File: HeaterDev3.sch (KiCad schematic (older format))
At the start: 27 parts, among them J1 USB_C_Receptacle_USB2.0, J9 Conn_01x04_Female, Q1 Q_NMOS_GSD, SW1 SW_SPST, U1 ATSAMD21E18A-MU, U2 FUSB302BMPX, U3 STS-30-DIS, U5 AP2112K-3.3

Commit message: Fixes and changes
Swapped USB
Changed heater to PA19
Removed APA102 and replaced with SK6812MINI on pin PA06
Changed soldermask clearence
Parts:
- removed D1: APA102, LED_SMD:LED_RGB_PLCC-6, symbol LED:APA102
- added D1: SK6812MINI, LED_SMD:LED_SK6812MINI_PLCC4_3.5x3.5mm_P1.75mm, symbol LED:SK6812MINI
- added R5, R6: 5.1k, Resistor_SMD:R_0603_1608Metric, symbol Device:R_Small
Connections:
- net labels added: NEOPIX_DAT
- wire segments 95 -> 102
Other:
- note added: "CC Resistors in case you just want to omit the PD chip."
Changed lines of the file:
@@
 Wire Wire Line
 	5050 3000 5000 3000
-$Comp
-L LED:APA102 D1
-U 1 1 5EA7B5CC
-P 2000 3600
-F 0 "D1" H 2150 3850 50  0000 C CNN
-F 1 "APA102" H 2150 3350 50  0000 C CNN
-F 2 "LED_SMD:LED_RGB_PLCC-6" H 2050 3300 50  0001 L TNN
-F 3 "http://www.led-color.com/upload/201506/APA102%20LED.pdf" H 2100 3225 50  0001 L TNN
-	1    2000 3600
-	1    0    0    -1
-$EndComp
 Wire Wire Line
 	3000 3300 2800 3300
 Wire Wire Line
 	2800 3300 2800 2850
-Wire Wire Line
-	3000 3500 2300 3500
-Wire Wire Line
-	3000 3600 2300 3600
-$Comp
-L power:+3V3 #PWR0105
-U 1 1 5EA810E9
-P 2000 3200
-F 0 "#PWR0105" H 2000 3050 50  0001 C CNN
-F 1 "+3V3" H 2050 3300 50  0000 L CNN
-F 2 "" H 2000 3200 50  0001 C CNN
-F 3 "" H 2000 3200 50  0001 C CNN
-	1    2000 3200
-	1    0    0    -1
-$EndComp
-Wire Wire Line
-	2000 3200 2000 3300
-$Comp
-L power:GND #PWR0106
-U 1 1 5EA82082
-P 2000 3950
-F 0 "#PWR0106" H 2000 3700 50  0001 C CNN
-F 1 "GND" H 2005 3777 50  0000 C CNN
-F 2 "" H 2000 3950 50  0001 C CNN
-F 3 "" H 2000 3950 50  0001 C CNN
-	1    2000 3950
-	1    0    0    -1
-$EndComp
-Wire Wire Line
-	2000 3900 2000 3950
 $Comp
 L Device:LED D2
@@
 	3450 -1600 3550 -1600
 Connection ~ 3450 -1600
+Text GLabel 3550 -1600 2    50   Input ~ 0
+D+
 Text GLabel 3550 -1700 2    50   Input ~ 0
-D+
-Text GLabel 3550 -1600 2    50   Input ~ 0
 D-
 $Comp
@@
 Wire Wire Line
 	5800 1200 5800 1250
-Text GLabel 2900 3700 0    50   Input ~ 0
+Text GLabel 4500 4300 2    50   Input ~ 0
 HEATER
 $Comp
@@
 Text Label 8600 4850 0    50   ~ 0
 COIL
+Text GLabel 3800 -2000 0    50   Input ~ 0
+CC2
+Text GLabel 3800 -2100 0    50   Input ~ 0
+CC1
+$Comp
+L Device:R_Small R5
+U 1 1 5EEB0FDB
+P 4000 -2100
+F 0 "R5" V 3900 -2100 50  0000 C CNN
+F 1 "5.1k" V 4000 -2100 31  0000 C CNN
+F 2 "Resistor_SMD:R_0603_1608Metric" H 4000 -2100 50  0001 C CNN
+F 3 "~" H 4000 -2100 50  0001 C CNN
+	1    4000 -2100
+	0    1    1    0
+$EndComp
+$Comp
+L Device:R_Small R6
+U 1 1 5EEB1A64
+P 4000 -2000
+F 0 "R6" V 4100 -2000 50  0000 C CNN
+F 1 "5.1k" V 4000 -2000 31  0000 C CNN
+F 2 "Resistor_SMD:R_0603_1608Metric" H 4000 -2000 50  0001 C CNN
+F 3 "~" H 4000 -2000 50  0001 C CNN
+	1    4000 -2000
+	0    1    1    0
+$EndComp
+Text Notes 4150 -1900 0    50   ~ 0
+CC Resistors in case you just want to omit the PD chip.
+$Comp
+L power:GND #PWR0138
+U 1 1 5EEB3038
+P 4200 -2100
+F 0 "#PWR0138" H 4200 -2350 50  0001 C CNN
+F 1 "GND" H 4205 -2273 50  0000 C CNN
+F 2 "" H 4200 -2100 50  0001 C CNN
+F 3 "" H 4200 -2100 50  0001 C CNN
+	1    4200 -2100
+	0    -1   -1   0
+$EndComp
+Wire Wire Line
+	4200 -2100 4150 -2100
+Wire Wire Line
+	4100 -2000 4150 -2000
+Wire Wire Line
+	4150 -2000 4150 -2100
+Connection ~ 4150 -2100
+Wire Wire Line
+	4150 -2100 4100 -2100
+Wire Wire Line
+	3900 -2100 3800 -2100
+Wire Wire Line
+	3900 -2000 3800 -2000
+$Comp
+L LED:SK6812MINI D1
+U 1 1 5EEF51C5
+P 1450 5400
+F 0 "D1" H 1794 5446 50  0000 L CNN
+F 1 "SK6812MINI" H 1794 5355 50  0000 L CNN
+F 2 "LED_SMD:LED_SK6812MINI_PLCC4_3.5x3.5mm_P1.75mm" H 1500 5100 50  0001 L TNN
+F 3 "https://cdn-shop.adafruit.com/product-files/2686/SK6812MINI_REV.01-1-2.pdf" H 1550 5025 50  0001 L TNN
+	1    1450 5400
+	1    0    0    -1
+$EndComp
+Text GLabel 2900 4100 0    50   Input ~ 0
+NEOPIX_DAT
+Wire Wire Line
+	3000 4100 2900 4100
+Wire Wire Line
+	4500 4300 4400 4300
+Text GLabel 1050 5400 0    50   Input ~ 0
+NEOPIX_DAT
+Wire Wire Line
+	1150 5400 1050 5400
+$Comp
+L power:GND #PWR0105
+U 1 1 5EF01523
+P 1450 5750
+F 0 "#PWR0105" H 1450 5500 50  0001 C CNN
+F 1 "GND" V 1455 5622 50  0000 R CNN
+F 2 "" H 1450 5750 50  0001 C CNN
+F 3 "" H 1450 5750 50  0001 C CNN
+	1    1450 5750
+	1    0    0    -1
+$EndComp
+$Comp
+L power:+3V3 #PWR0106
+U 1 1 5EF01E84
+P 1450 4900
+F 0 "#PWR0106" H 1450 4750 50  0001 C CNN
+F 1 "+3V3" V 1350 4650 50  0000 L CNN
+F 2 "" H 1450 4900 50  0001 C CNN
+F 3 "" H 1450 4900 50  0001 C CNN
+	1    1450 4900
+	1    0    0    -1
+$EndComp
+Wire Wire Line
+	1450 4900 1450 5100
+Wire Wire Line
+	1450 5700 1450 5750
 $EndSCHEMATC

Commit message: Added Temperature Cutoff Circuit
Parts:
- removed Q1: Q_NMOS_GSD, Package_TO_SOT_SMD:SOT-223-3_TabPin2, symbol Device:Q_NMOS_GSD
- added D3: LED, Capacitor_SMD:C_0603_1608Metric, symbol Device:LED
- added Q1: Q_NMOS_GDS, Package_TO_SOT_SMD:SOT-223-3_TabPin2, symbol Device:Q_NMOS_GDS
- added R10, R11, R12: 10k, Resistor_SMD:R_0603_1608Metric, symbol Device:R_Small
- added R13: 1.5k, Resistor_SMD:R_0603_1608Metric, symbol Device:R_Small
- added R7, R9: 4.7k, Resistor_SMD:R_0603_1608Metric, symbol Device:R_Small
- added R8: NTC, Resistor_SMD:R_0603_1608Metric, symbol Device:R_Small
- added U4: LM393, Package_DFN_QFN:DFN-8-1EP_2x2mm_P0.45mm_EP0.64x1.38mm, symbol Comparator:LM393
- R3, R4: value 1.5k -> 10k
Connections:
- net labels added: ELEMENT_GATE
- wire segments 102 -> 130
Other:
- note added: "3.024k at 60c\n10k at 25c\n2.2v vdiv when at 60c and R7 is 1.5k\nfor cutoff at 40 use 2.5k\nfor cutoff at 50 use 2k"
- note added: "TH voltage 2.2v"

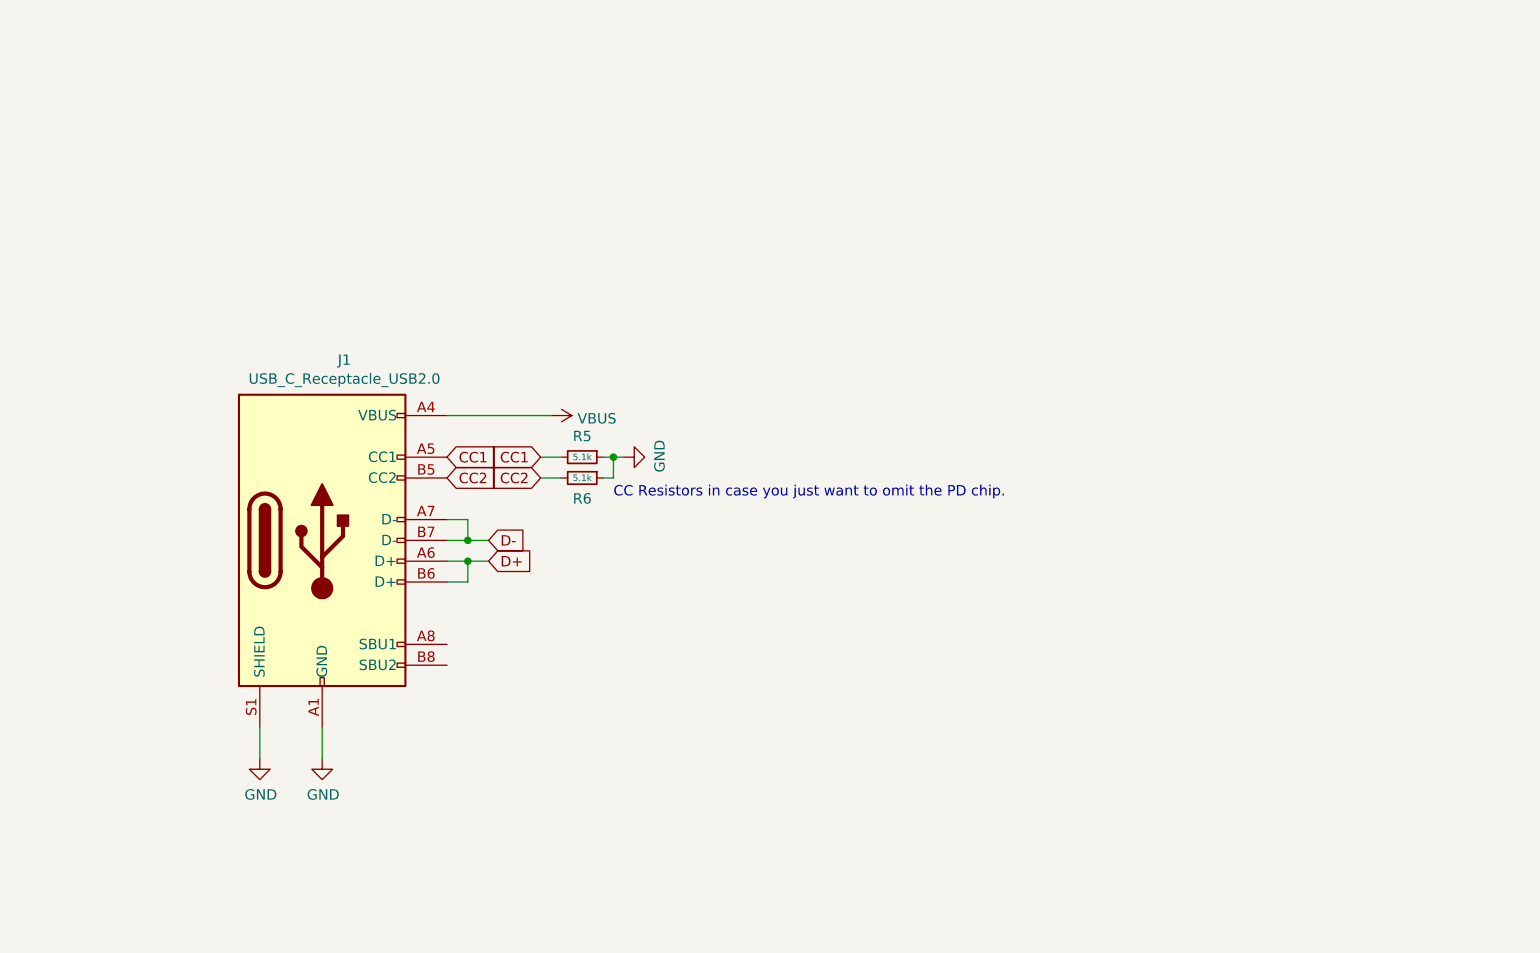
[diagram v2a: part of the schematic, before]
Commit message: Swapped out USB Connector for a simpler version.
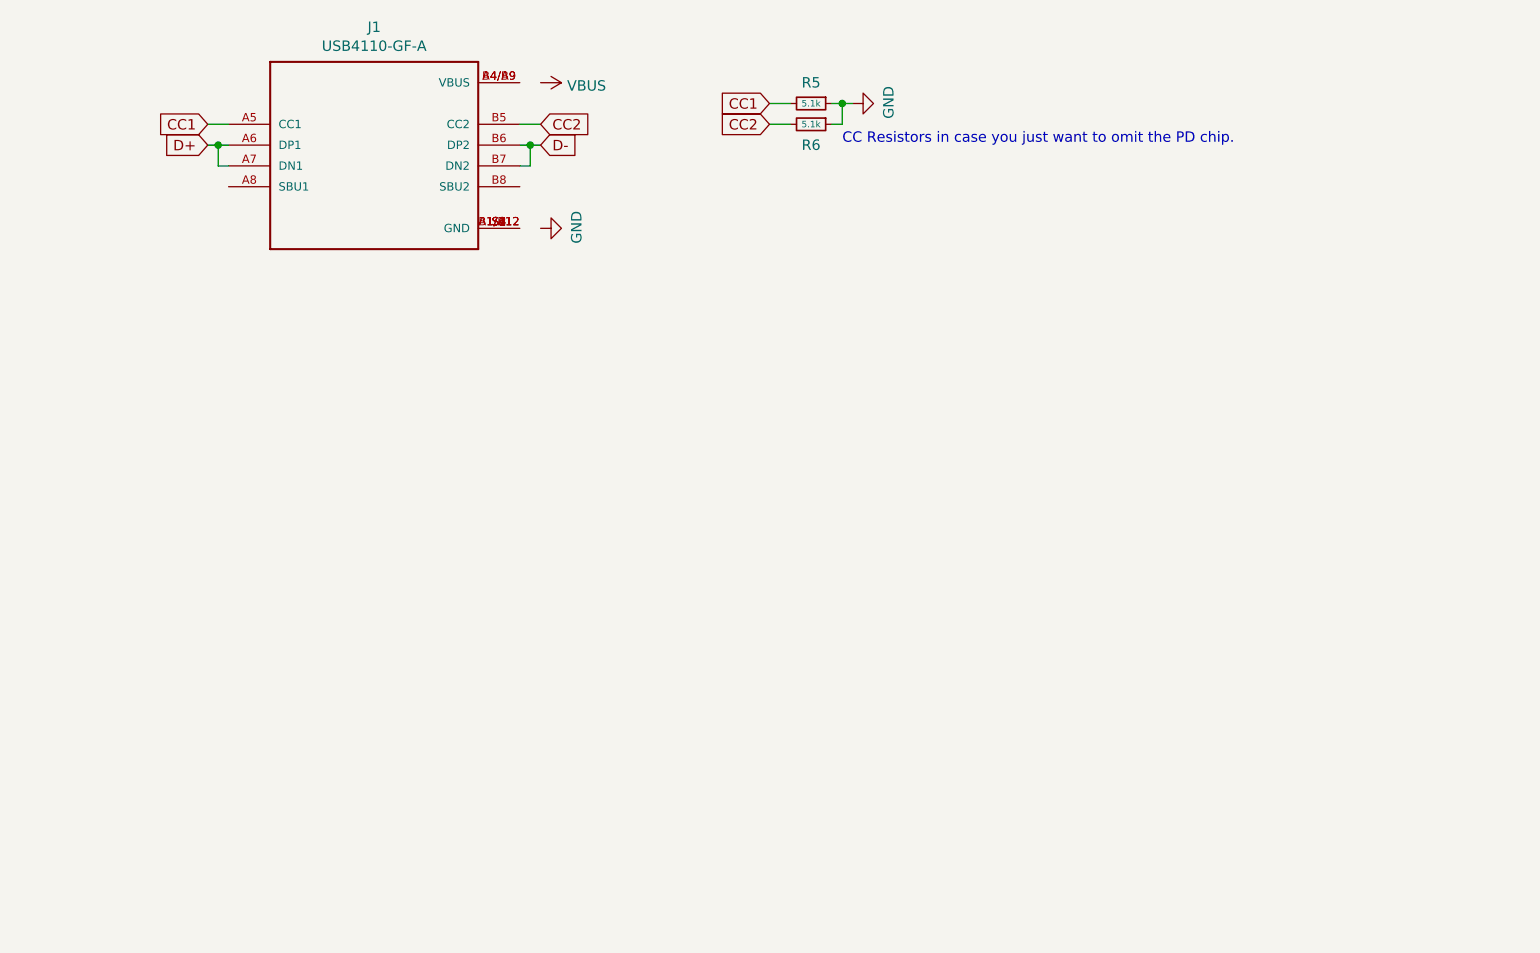
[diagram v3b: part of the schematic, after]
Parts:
- removed J1: USB_C_Receptacle_USB2.0, Connector_USB:USB_C_Receptacle_Amphenol_12401610E4-2A, symbol Connector:USB_C_Receptacle_USB2.0
- added J1: USB4110-GF-A, HeaterDev3:GCT_USB4110-GF-A, symbol USB4110-GF-A:USB4110-GF-A
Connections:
- wire segments 130 -> 129
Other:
- moved on the sheet: R5, R6
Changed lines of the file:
@@
 Connection ~ 10350 -1350
-$Comp
-L Connector:USB_C_Receptacle_USB2.0 J1
-U 1 1 5EAB43F1
-P 2750 -1700
-F 0 "J1" H 2857 -833 50  0000 C CNN
-F 1 "USB_C_Receptacle_USB2.0" H 2857 -924 50  0000 C CNN
-F 2 "Connector_USB:USB_C_Receptacle_Amphenol_12401610E4-2A" H 2900 -1700 50  0001 C CNN
-F 3 "https://www.usb.org/sites/default/files/documents/usb_type-c.zip" H 2900 -1700 50  0001 C CNN
-	1    2750 -1700
-	1    0    0    -1
-$EndComp
 $Comp
 L Device:C_Small C4
@@
 Text GLabel 2950 4300 0    50   Input ~ 0
 SDA
-Wire Wire Line
-	3350 -1800 3450 -1800
-Wire Wire Line
-	3450 -1800 3450 -1700
-Wire Wire Line
-	3450 -1700 3350 -1700
-Wire Wire Line
-	3450 -1600 3450 -1500
-Wire Wire Line
-	3350 -1500 3450 -1500
-Wire Wire Line
-	3350 -1600 3450 -1600
-Wire Wire Line
-	3450 -1700 3550 -1700
-Connection ~ 3450 -1700
-Wire Wire Line
-	3450 -1600 3550 -1600
-Connection ~ 3450 -1600
-Text GLabel 3550 -1600 2    50   Input ~ 0
-D+
-Text GLabel 3550 -1700 2    50   Input ~ 0
-D-
 $Comp
 L power:+3V3 #PWR0111
@@
 Wire Wire Line
 	10650 -1950 10650 -1850
-Text GLabel 3350 -2100 2    50   Input ~ 0
+Text GLabel 2200 -3700 0    50   Input ~ 0
 CC1
-Text GLabel 3350 -2000 2    50   Input ~ 0
+Text GLabel 3800 -3700 2    50   Input ~ 0
 CC2
 Text GLabel 2350 1250 2    50   Input ~ 0
@@
 Wire Wire Line
 	2900 3700 3000 3700
-$Comp
-L power:GND #PWR0124
-U 1 1 5EECBAEE
-P 2750 -650
-F 0 "#PWR0124" H 2750 -900 50  0001 C CNN
-F 1 "GND" H 2755 -823 50  0000 C CNN
-F 2 "" H 2750 -650 50  0001 C CNN
-F 3 "" H 2750 -650 50  0001 C CNN
-	1    2750 -650
-	1    0    0    -1
-$EndComp
-$Comp
-L power:GND #PWR0125
-U 1 1 5EECC53B
-P 2450 -650
-F 0 "#PWR0125" H 2450 -900 50  0001 C CNN
-F 1 "GND" H 2455 -823 50  0000 C CNN
-F 2 "" H 2450 -650 50  0001 C CNN
-F 3 "" H 2450 -650 50  0001 C CNN
-	1    2450 -650
-	1    0    0    -1
-$EndComp
-Wire Wire Line
-	2750 -800 2750 -650
-Wire Wire Line
-	2450 -800 2450 -650
 $Comp
 L Mechanical:MountingHole H3
@@
 L power:VBUS #PWR0112
 U 1 1 5ECB229D
-P 3850 -2300
-F 0 "#PWR0112" H 3850 -2450 50  0001 C CNN
-F 1 "VBUS" V 3865 -2173 50  0000 L CNN
-F 2 "" H 3850 -2300 50  0001 C CNN
-F 3 "" H 3850 -2300 50  0001 C CNN
-	1    3850 -2300
-	0    1    1    0
-$EndComp
-Wire Wire Line
-	3350 -2300 3850 -2300
+P 3800 -3900
+F 0 "#PWR0112" H 3800 -4050 50  0001 C CNN
+F 1 "VBUS" V 3815 -3773 50  0000 L CNN
+F 2 "" H 3800 -3900 50  0001 C CNN
+F 3 "" H 3800 -3900 50  0001 C CNN
+	1    3800 -3900
+	0    1    1    0
+$EndComp
 $Comp
 L Interface_USB:FUSB302BMPX U2
@@
 Text Label 8600 4850 0    50   ~ 0
 COIL
-Text GLabel 3800 -2000 0    50   Input ~ 0
+Text GLabel 4900 -3700 0    50   Input ~ 0
 CC2
-Text GLabel 3800 -2100 0    50   Input ~ 0
+Text GLabel 4900 -3800 0    50   Input ~ 0
 CC1
 $Comp
 L Device:R_Small R5
 U 1 1 5EEB0FDB
-P 4000 -2100
-F 0 "R5" V 3900 -2100 50  0000 C CNN
-F 1 "5.1k" V 4000 -2100 31  0000 C CNN
-F 2 "Resistor_SMD:R_0603_1608Metric" H 4000 -2100 50  0001 C CNN
-F 3 "~" H 4000 -2100 50  0001 C CNN
-	1    4000 -2100
+P 5100 -3800
+F 0 "R5" V 5000 -3800 50  0000 C CNN
+F 1 "5.1k" V 5100 -3800 31  0000 C CNN
+F 2 "Resistor_SMD:R_0603_1608Metric" H 5100 -3800 50  0001 C CNN
+F 3 "~" H 5100 -3800 50  0001 C CNN
+	1    5100 -3800
 	0    1    1    0
 $EndComp
@@
 L Device:R_Small R6
 U 1 1 5EEB1A64
-P 4000 -2000
-F 0 "R6" V 4100 -2000 50  0000 C CNN
-F 1 "5.1k" V 4000 -2000 31  0000 C CNN
-F 2 "Resistor_SMD:R_0603_1608Metric" H 4000 -2000 50  0001 C CNN
-F 3 "~" H 4000 -2000 50  0001 C CNN
-	1    4000 -2000
-	0    1    1    0
-$EndComp
-Text Notes 4150 -1900 0    50   ~ 0
+P 5100 -3700
+F 0 "R6" V 5200 -3700 50  0000 C CNN
+F 1 "5.1k" V 5100 -3700 31  0000 C CNN
+F 2 "Resistor_SMD:R_0603_1608Metric" H 5100 -3700 50  0001 C CNN
+F 3 "~" H 5100 -3700 50  0001 C CNN
+	1    5100 -3700
+	0    1    1    0
+$EndComp
+Text Notes 5250 -3600 0    50   ~ 0
 CC Resistors in case you just want to omit the PD chip.
 $Comp
 L power:GND #PWR0138
 U 1 1 5EEB3038
-P 4200 -2100
-F 0 "#PWR0138" H 4200 -2350 50  0001 C CNN
-F 1 "GND" H 4205 -2273 50  0000 C CNN
-F 2 "" H 4200 -2100 50  0001 C CNN
-F 3 "" H 4200 -2100 50  0001 C CNN
-	1    4200 -2100
+P 5300 -3800
+F 0 "#PWR0138" H 5300 -4050 50  0001 C CNN
+F 1 "GND" H 5305 -3973 50  0000 C CNN
+F 2 "" H 5300 -3800 50  0001 C CNN
+F 3 "" H 5300 -3800 50  0001 C CNN
+	1    5300 -3800
 	0    -1   -1   0
 $EndComp
 Wire Wire Line
-	4200 -2100 4150 -2100
-Wire Wire Line
-	4100 -2000 4150 -2000
-Wire Wire Line
-	4150 -2000 4150 -2100
-Connection ~ 4150 -2100
-Wire Wire Line
-	4150 -2100 4100 -2100
-Wire Wire Line
-	3900 -2100 3800 -2100
-Wire Wire Line
-	3900 -2000 3800 -2000
+	5300 -3800 5250 -3800
+Wire Wire Line
+	5200 -3700 5250 -3700
+Wire Wire Line
+	5250 -3700 5250 -3800
+Connection ~ 5250 -3800
+Wire Wire Line
+	5250 -3800 5200 -3800
+Wire Wire Line
+	5000 -3800 4900 -3800
+Wire Wire Line
+	5000 -3700 4900 -3700
 $Comp
 L LED:SK6812MINI D1
@@
 Wire Wire Line
 	7150 10200 7100 10200
+$Comp
+L USB4110-GF-A:USB4110-GF-A J1
+U 1 1 5EF03D48
+P 3000 -3600
+F 0 "J1" H 3000 -3033 50  0000 C CNN
+F 1 "USB4110-GF-A" H 3000 -3124 50  0000 C CNN
+F 2 "HeaterDev3:GCT_USB4110-GF-A" H 3000 -3600 50  0001 L BNN
+F 3 "" H 3000 -3600 50  0001 L BNN
+F 4 "A" H 3000 -3600 50  0001 L BNN "Field4"
+F 5 "GCT" H 3000 -3600 50  0001 L BNN "Field5"
+F 6 "Manufacturer Recommendations" H 3000 -3600 50  0001 L BNN "Field6"
+	1    3000 -3600
+	1    0    0    -1
+$EndComp
+Text GLabel 2200 -3600 0    50   Input ~ 0
+D+
+Text GLabel 3800 -3600 2    50   Input ~ 0
+D-
+Wire Wire Line
+	3700 -3700 3800 -3700
+Wire Wire Line
+	2200 -3700 2300 -3700
+Wire Wire Line
+	2300 -3600 2250 -3600
+Wire Wire Line
+	3800 -3600 3750 -3600
+Wire Wire Line
+	2250 -3600 2250 -3500
+Wire Wire Line
+	2250 -3500 2300 -3500
+Connection ~ 2250 -3600
+Wire Wire Line
+	2250 -3600 2200 -3600
+Wire Wire Line
+	3700 -3500 3750 -3500
+Wire Wire Line
+	3750 -3500 3750 -3600
+Connection ~ 3750 -3600
+Wire Wire Line
+	3750 -3600 3700 -3600
+$Comp
+L power:GND #PWR0124
+U 1 1 5EF357BE
+P 3800 -3200
+F 0 "#PWR0124" H 3800 -3450 50  0001 C CNN
+F 1 "GND" H 3805 -3373 50  0000 C CNN
+F 2 "" H 3800 -3200 50  0001 C CNN
+F 3 "" H 3800 -3200 50  0001 C CNN
+	1    3800 -3200
+	0    -1   -1   0
+$EndComp
 $EndSCHEMATC

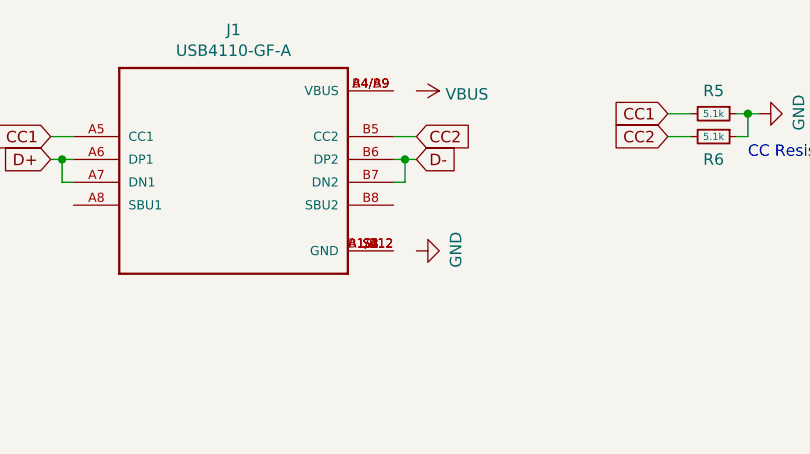
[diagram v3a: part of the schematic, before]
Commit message: Cleaned up routing.
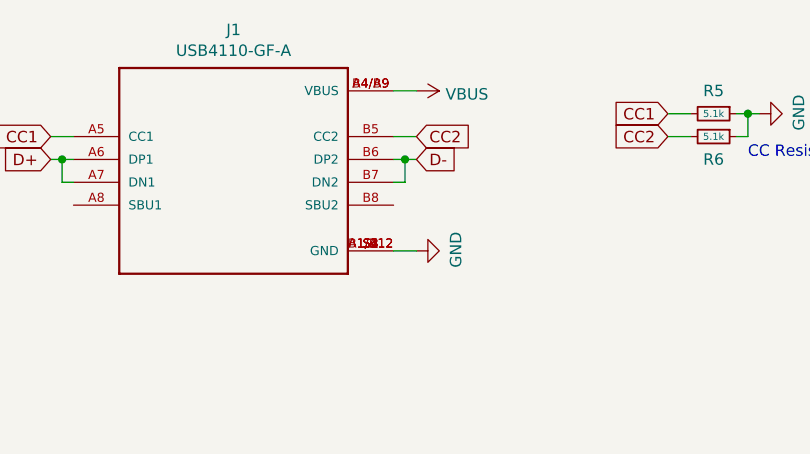
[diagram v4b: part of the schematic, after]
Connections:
- wire segments 129 -> 131
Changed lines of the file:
@@
 	0    -1   -1   0
 $EndComp
+Wire Wire Line
+	3800 -3900 3700 -3900
+Wire Wire Line
+	3800 -3200 3700 -3200
 $EndSCHEMATC
